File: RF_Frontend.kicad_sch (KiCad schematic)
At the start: 60 parts, among them IC2 SX1280, J3 Conn_01x03_Pin, U11 SC4215ASTRT, U12 SKY66112-11, U13 DEA202450BT-1213C1, U6 DEA202450BT-1213C1, Y3 Crystal_GND24

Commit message: Tidying up
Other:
- note removed: "I'm not smart enough to know when to split or not split grounds"
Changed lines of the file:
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@@
 	)
 	(junction
-		(at 118.11 172.72)
+		(at 142.24 163.83)
 		(diameter 0)
 		(color 0 0 0 0)
@@
 	(wire
 		(pts
-			(xy 111.76 172.72) (xy 118.11 172.72)
+			(xy 135.89 163.83) (xy 142.24 163.83)
 		)
 		(stroke
@@
 	(wire
 		(pts
-			(xy 118.11 172.72) (xy 124.46 172.72)
+			(xy 142.24 163.83) (xy 148.59 163.83)
 		)
 		(stroke
@@
 		)
 	)
-	(text "I'm not smart enough to know when to split or not split grounds\n"
-		(exclude_from_sim no)
-		(at 118.364 170.434 0)
-		(effects
-			(font
-				(size 1.27 1.27)
-			)
-		)
-	)
 	(label "FBIn"
 		(at 208.28 40.64 180)
@@
 	(symbol
 		(lib_id "power:GNDS")
-		(at 111.76 172.72 0)
+		(at 135.89 163.83 0)
 		(unit 1)
 		(exclude_from_sim no)
@@
 		(fields_autoplaced yes)
 		(property "Reference" "#PWR046"
-			(at 111.76 179.07 0)
+			(at 135.89 170.18 0)
 			(effects
 				(font
@@
 		)
 		(property "Value" "GNDS"
-			(at 111.76 177.8 0)
+			(at 135.89 168.91 0)
 			(effects
 				(font
@@
 		)
 		(property "Footprint" ""
-			(at 111.76 172.72 0)
+			(at 135.89 163.83 0)
 			(effects
 				(font
@@
 		)
 		(property "Datasheet" ""
-			(at 111.76 172.72 0)
+			(at 135.89 163.83 0)
 			(effects
 				(font
@@
 		)
 		(property "Description" "Power symbol creates a global label with name \"GNDS\" , signal ground"
-			(at 111.76 172.72 0)
+			(at 135.89 163.83 0)
 			(effects
 				(font
@@
 	(symbol
 		(lib_id "power:GND")
-		(at 124.46 172.72 0)
+		(at 148.59 163.83 0)
 		(unit 1)
 		(exclude_from_sim no)
@@
 		(fields_autoplaced yes)
 		(property "Reference" "#PWR051"
-			(at 124.46 179.07 0)
+			(at 148.59 170.18 0)
 			(effects
 				(font
@@
 		)
 		(property "Value" "GND"
-			(at 124.46 177.8 0)
+			(at 148.59 168.91 0)
 			(effects
 				(font
@@
 		)
 		(property "Footprint" ""
-			(at 124.46 172.72 0)
+			(at 148.59 163.83 0)
 			(effects
 				(font
@@
 		)
 		(property "Datasheet" ""
-			(at 124.46 172.72 0)
+			(at 148.59 163.83 0)
 			(effects
 				(font
@@
 		)
 		(property "Description" ""
-			(at 124.46 172.72 0)
+			(at 148.59 163.83 0)
 			(effects
 				(font
@@
 	(symbol
 		(lib_id "power:GNDA")
-		(at 118.11 172.72 0)
+		(at 142.24 163.83 0)
 		(unit 1)
 		(exclude_from_sim no)
@@
 		(fields_autoplaced yes)
 		(property "Reference" "#PWR049"
-			(at 118.11 179.07 0)
+			(at 142.24 170.18 0)
 			(effects
 				(font
@@
 		)
 		(property "Value" "GNDA"
-			(at 118.11 177.8 0)
+			(at 142.24 168.91 0)
 			(effects
 				(font
@@
 		)
 		(property "Footprint" ""
-			(at 118.11 172.72 0)
+			(at 142.24 163.83 0)
 			(effects
 				(font
@@
 		)
 		(property "Datasheet" ""
-			(at 118.11 172.72 0)
+			(at 142.24 163.83 0)
 			(effects
 				(font
@@
 		)
 		(property "Description" "Power symbol creates a global label with name \"GNDA\" , analog ground"
-			(at 118.11 172.72 0)
+			(at 142.24 163.83 0)
 			(effects
 				(font

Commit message: Finishing touches without BOM
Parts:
- removed CS1, MISO1, MOSI1, SCK1: TestPoint, TestPoint:TestPoint_Pad_D1.0mm, symbol Connector:TestPoint
- removed U13, U6: DEA202450BT-1213C1, iclr:DEA-4_2P0X1P25, symbol iclr:DEA202450BT-1213C1
- added C77: 0.4 pF, Capacitor_SMD:C_0402_1005Metric, symbol Device:C_Small
- added C78, C80: 1.2 pF, Capacitor_SMD:C_0402_1005Metric, symbol Device:C_Small
- added C79: 0.5 pF, Capacitor_SMD:C_0402_1005Metric, symbol Device:C_Small
- added L7: DET_LATER, Inductor_SMD:L_0402_1005Metric, symbol Device:L
- added L8: 0.5 pF, Inductor_SMD:L_0402_1005Metric, symbol Device:L
- FB_R1: value FerriteBead_Small -> FB
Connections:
- net GND: now also C77.2, C78.2, C80.2
- net RF_OUT_T: now also C79.1, C80.1, L8.2; no longer IC2.22 (RFIO)
- net at U12.6 (ANT2): now also ANT2.1 (In)
- net at ANT1.1 (In): now also U12.8 (ANT1)
- new net: C77.1, IC2.22 (RFIO), L7.1
- new net: C78.1, C79.2, L7.2, L8.1
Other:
- note added: "Power"
- note added: "Test and Debugging"
- note removed: "Choose sth that filters around 2.4ghz..."
- moved on the sheet: ANT1, ANT2, ANT_S1, BUSY1, C12, C18, C19, C50, C51, C52, C53, C54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

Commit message: finishing changes
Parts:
- DIO3_D1: value GREEN_LED -> BLUE_LED; footprint Resistor_SMD:R_0402_1005Metric -> Diode_SMD:D_0402_1005Metric
- L4: footprint Capacitor_SMD:C_0603_1608Metric -> Inductor_SMD:L_0603_1608Metric
- L7: value DET_LATER -> 3.0 nH
- R31, R32, R33, R34: value 20-100 -> 50
- RXD_1_R1: renamed from RXD_1; value GREEN_LED -> ORANGE_LED; footprint Resistor_SMD:R_0402_1005Metric -> Diode_SMD:D_0402_1005Metric
- TXD_1_R1: renamed from TXD_1; footprint Resistor_SMD:R_0402_1005Metric -> Diode_SMD:D_0402_1005Metric
- Y3: value Crystal_GND24 -> Crystal_GND24_52_MHZ
- renumbered ANT1 to ANT_SMA1, ANT2 to ANT_UFL1, R35 to VCC_SX1
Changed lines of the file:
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@@
 		(dnp no)
 		(fields_autoplaced yes)
-		(property "Reference" "ANT2"
-			(at 255.27 133.6431 0)
+		(property "Reference" "ANT_UFL1"
+			(at 255.2701 133.701 0)
 			(effects
 				(font
@@
 		)
 		(property "Value" "u.FL"
-			(at 255.27 136.1831 0)
+			(at 255.2701 136.1253 0)
 			(effects
 				(font
@@
 			(project "Ricardo-Hermes"
 				(path "/7db990e4-92e1-4f99-b4d2-435bbec1ba83/ecfc1314-a0cb-4bac-a35c-d2175f1c7197"
-					(reference "ANT2")
+					(reference "ANT_UFL1")
 					(unit 1)
 				)
@@
 		(on_board yes)
 		(dnp no)
-		(property "Reference" "ANT1"
+		(property "Reference" "ANT_SMA1"
 			(at 255.27 150.8369 0)
 			(effects
@@
 			(project "RicardoTemplate"
 				(path "/7db990e4-92e1-4f99-b4d2-435bbec1ba83/ecfc1314-a0cb-4bac-a35c-d2175f1c7197"
-					(reference "ANT1")
+					(reference "ANT_SMA1")
 					(unit 1)
 				)
@@
 			)
 		)
-		(property "Footprint" "Capacitor_SMD:C_0603_1608Metric"
+		(property "Footprint" "Inductor_SMD:L_0603_1608Metric"
 			(at 102.87 76.2 0)
 			(effects
@@
 			)
 		)
-		(property "Value" "20-100"
+		(property "Value" "50"
 			(at 111.76 54.61 90)
 			(effects
@@
 		(on_board yes)
 		(dnp no)
-		(property "Reference" "RXD_1"
+		(property "Reference" "RXD_1_R1"
 			(at 73.66 136.017 0)
 			(effects
@@
 			)
 		)
-		(property "Value" "GREEN_LED"
+		(property "Value" "ORANGE_LED"
 			(at 73.66 133.7056 0)
 			(effects
@@
 			)
 		)
-		(property "Footprint" "Resistor_SMD:R_0402_1005Metric"
+		(property "Footprint" "Diode_SMD:D_0402_1005Metric"
 			(at 73.66 130.81 90)
 			(effects
@@
 			(project "Ricardo-Hermes"
 				(path "/7db990e4-92e1-4f99-b4d2-435bbec1ba83/ecfc1314-a0cb-4bac-a35c-d2175f1c7197"
-					(reference "RXD_1")
+					(reference "RXD_1_R1")
 					(unit 1)
 				)
@@
 			)
 		)
-		(property "Value" "Crystal_GND24"
+		(property "Value" "Crystal_GND24_52_MHZ"
 			(at 45.72 70.104 90)
 			(effects
@@
 			)
 		)
-		(property "Value" "20-100"
+		(property "Value" "50"
 			(at 111.76 52.07 90)
 			(effects
@@
 		(on_board yes)
 		(dnp no)
-		(property "Reference" "R35"
-			(at 91.948 88.9 90)
+		(property "Reference" "VCC_SX1"
+			(at 93.726 88.9 90)
 			(effects
 				(font
@@
 			(project "Ricardo-Hermes"
 				(path "/7db990e4-92e1-4f99-b4d2-435bbec1ba83/ecfc1314-a0cb-4bac-a35c-d2175f1c7197"
-					(reference "R35")
+					(reference "VCC_SX1")
 					(unit 1)
 				)
@@
 			)
 		)
-		(property "Value" "20-100"
+		(property "Value" "50"
 			(at 111.76 46.99 90)
 			(effects
@@
 			)
 		)
-		(property "Value" "GREEN_LED"
+		(property "Value" "BLUE_LED"
 			(at 73.66 143.8656 0)
 			(effects
@@
 			)
 		)
-		(property "Footprint" "Resistor_SMD:R_0402_1005Metric"
+		(property "Footprint" "Diode_SMD:D_0402_1005Metric"
 			(at 73.66 140.97 90)
 			(effects
@@
 			)
 		)
-		(property "Value" "20-100"
+		(property "Value" "50"
 			(at 111.76 49.53 90)
 			(effects
@@
 		(fields_autoplaced yes)
 		(property "Reference" "L7"
-			(at 170.18 52.07 90)
+			(at 170.18 52.5002 90)
 			(effects
 				(font
@@
 			)
 		)
-		(property "Value" "DET_LATER"
-			(at 170.18 54.61 90)
+		(property "Value" "3.0 nH"
+			(at 170.18 54.9245 90)
 			(effects
 				(font
@@
 		(on_board yes)
 		(dnp no)
-		(property "Reference" "TXD_1"
+		(property "Reference" "TXD_1_R1"
 			(at 73.66 125.857 0)
 			(effects
@@
 			)
 		)
-		(property "Footprint" "Resistor_SMD:R_0402_1005Metric"
+		(property "Footprint" "Diode_SMD:D_0402_1005Metric"
 			(at 73.66 120.65 90)
 			(effects
@@
 			(project "Ricardo-Hermes"
 				(path "/7db990e4-92e1-4f99-b4d2-435bbec1ba83/ecfc1314-a0cb-4bac-a35c-d2175f1c7197"
-					(reference "TXD_1")
+					(reference "TXD_1_R1")
 					(unit 1)
 				)

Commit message: Prod Files
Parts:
- C50, C51: value C_Small -> 15pF
- FB_R1: value FB -> C3011209
- L8: value 0.5 pF -> 2.5nH
- Y3: value Crystal_GND24_52_MHZ -> C3034316
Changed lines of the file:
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@@
 			)
 		)
-		(property "Value" "C_Small"
+		(property "Value" "15pF"
 			(at 30.48 59.69 90)
 			(effects
@@
 			)
 		)
-		(property "Value" "C_Small"
+		(property "Value" "15pF"
 			(at 30.48 67.31 90)
 			(effects
@@
 			)
 		)
-		(property "Value" "0.5 pF"
+		(property "Value" "2.5nH"
 			(at 191.77 52.578 90)
 			(effects
@@
 			)
 		)
-		(property "Value" "Crystal_GND24_52_MHZ"
+		(property "Value" "C3034316"
 			(at 45.72 70.104 90)
 			(effects
@@
 			)
 		)
-		(property "Value" "FB"
+		(property "Value" "C3011209"
 			(at 271.7419 20.32 90)
 			(effects

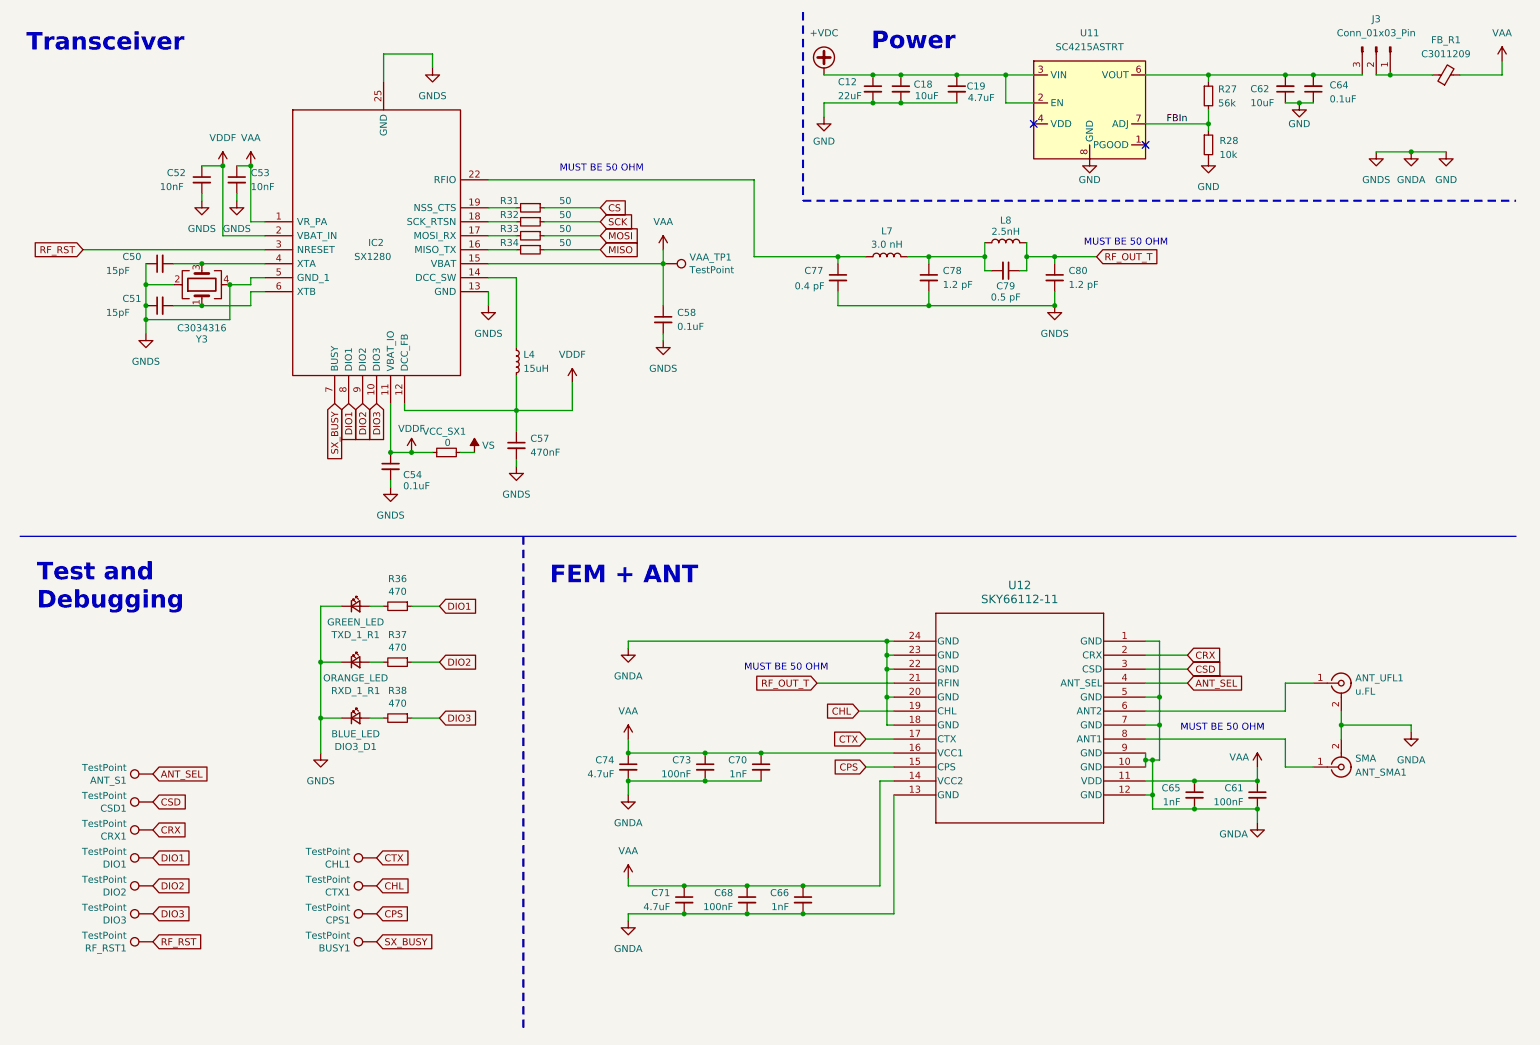
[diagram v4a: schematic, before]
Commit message: Went for a 3v3 plane
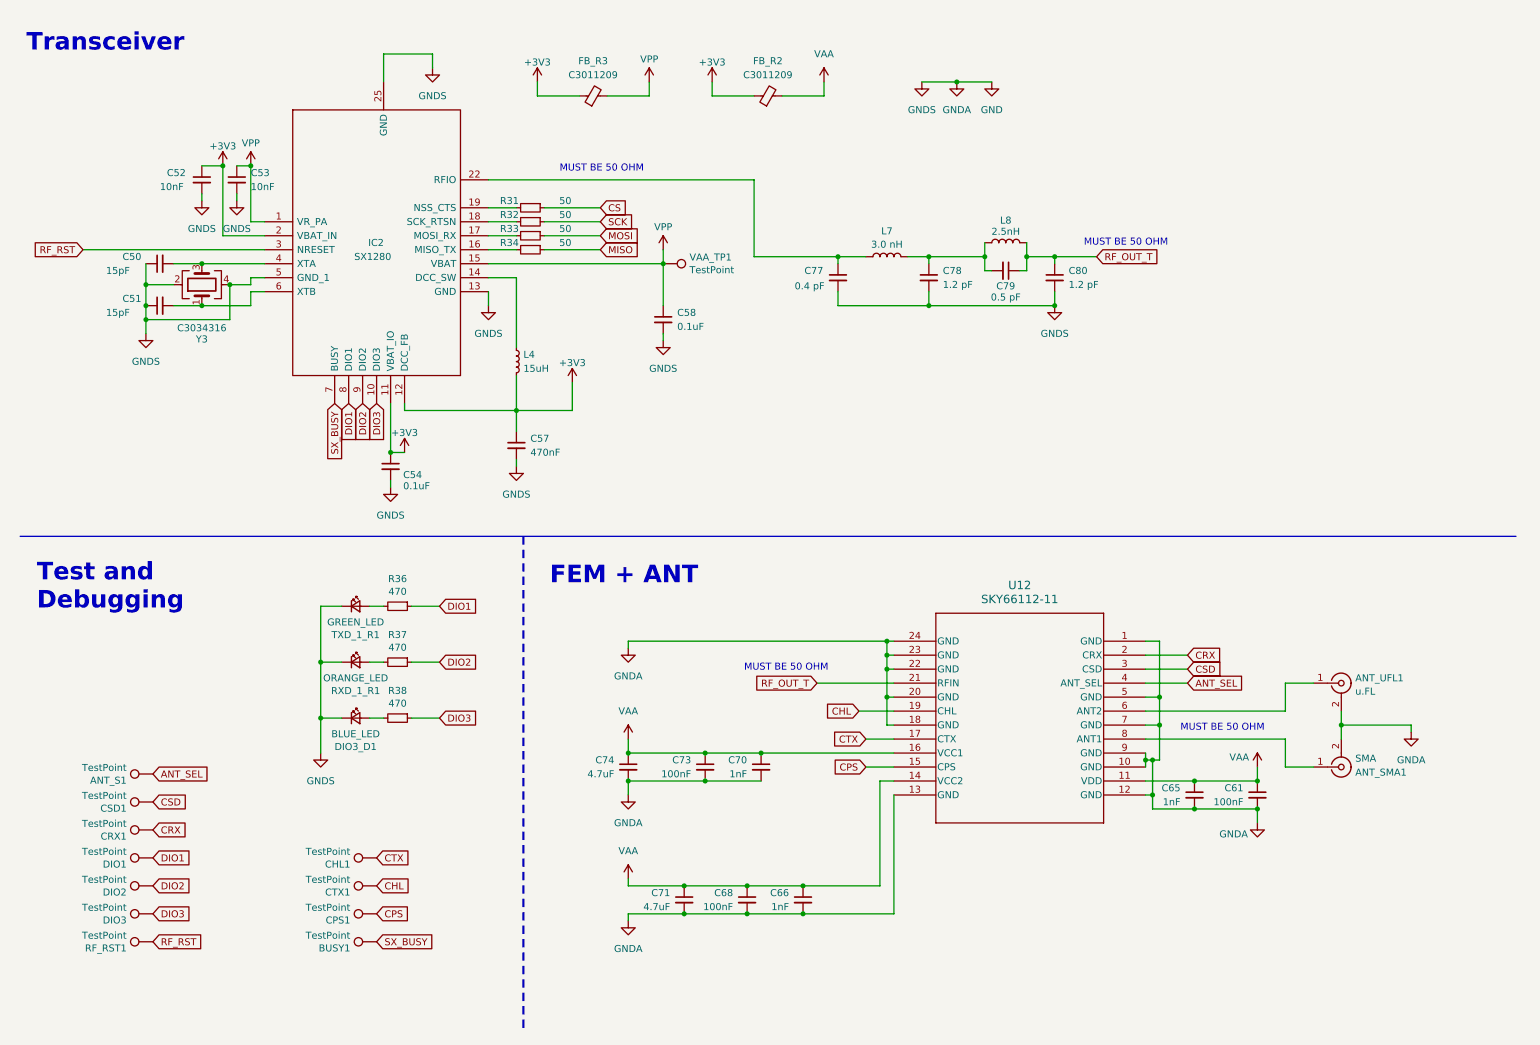
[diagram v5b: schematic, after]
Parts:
- removed C12: 22uF, Capacitor_SMD:C_0603_1608Metric, symbol Device:C_Small
- removed C18, C62: 10uF, Capacitor_SMD:C_0402_1005Metric, symbol Device:C_Small
- removed C19: 4.7uF, Capacitor_SMD:C_0402_1005Metric, symbol Device:C_Small
- removed C64: 0.1uF, Capacitor_SMD:C_0402_1005Metric, symbol Device:C_Small
- removed FB_R1: C3011209, Inductor_SMD:L_0603_1608Metric, symbol Device:FerriteBead_Small
- removed J3: Conn_01x03_Pin, Connector_PinHeader_2.54mm:PinHeader_1x03_P2.54mm_Vertical, symbol Connector:Conn_01x03_Pin
- removed R27: 56k, Resistor_SMD:R_0402_1005Metric, symbol Device:R_Small
- removed R28: 10k, Resistor_SMD:R_0402_1005Metric, symbol Device:R_Small
- removed U11: SC4215ASTRT, iclr:SOIC127P599X175-9N, symbol iclr:SC4215ASTRT
- removed VCC_SX1: 0, Resistor_SMD:R_0603_1608Metric, symbol Device:R_Small
- added FB_R2, FB_R3: C3011209, Inductor_SMD:L_0603_1608Metric, symbol Device:FerriteBead_Small
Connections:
- net VAA: now also FB_R2.2; no longer C53.1, C58.1, IC2.1 (VR_PA), IC2.15 (VBAT), VAA_TP1.1
- net VDDF renamed +3V3
- net +3V3: now also FB_R2.1, FB_R3.1
- new net VPP: C53.1, C58.1, FB_R3.2, IC2.1 (VR_PA), IC2.15 (VBAT), VAA_TP1.1
- no-connect marks 2 -> 0
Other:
- note removed: "Power"

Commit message: PCB status: unfucked
+ sick art
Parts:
- removed L4: 15uH, Inductor_SMD:L_0603_1608Metric, symbol Device:L_Small
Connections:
- net +3V3: no longer C52.1, C57.1, IC2.12 (DCC_FB), IC2.2 (VBAT_IN)
- net VPP: no longer C53.1, IC2.1 (VR_PA)
- new net: C53.1, IC2.1 (VR_PA)
- new net: C52.1, C57.1, IC2.12 (DCC_FB), IC2.2 (VBAT_IN)
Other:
- moved on the sheet: C57
